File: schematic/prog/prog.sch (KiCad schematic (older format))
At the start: 24 parts

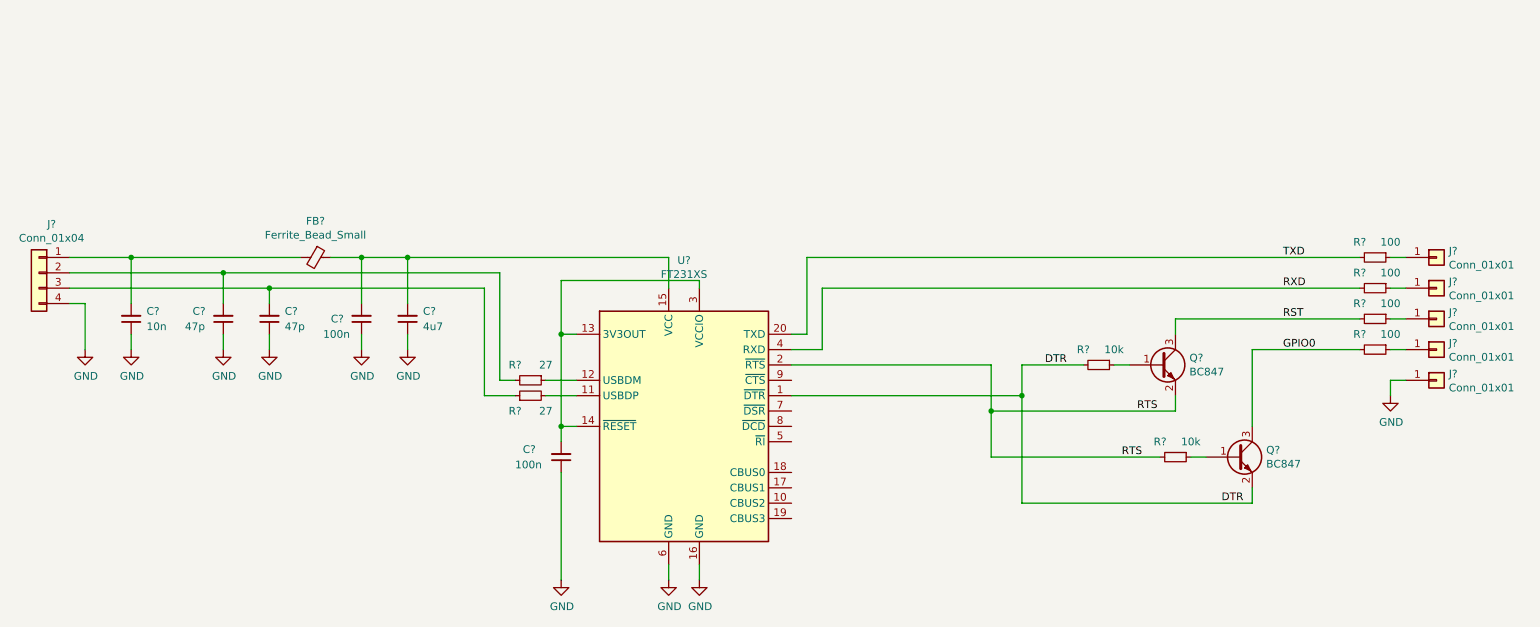
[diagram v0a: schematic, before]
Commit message: programing connector layout
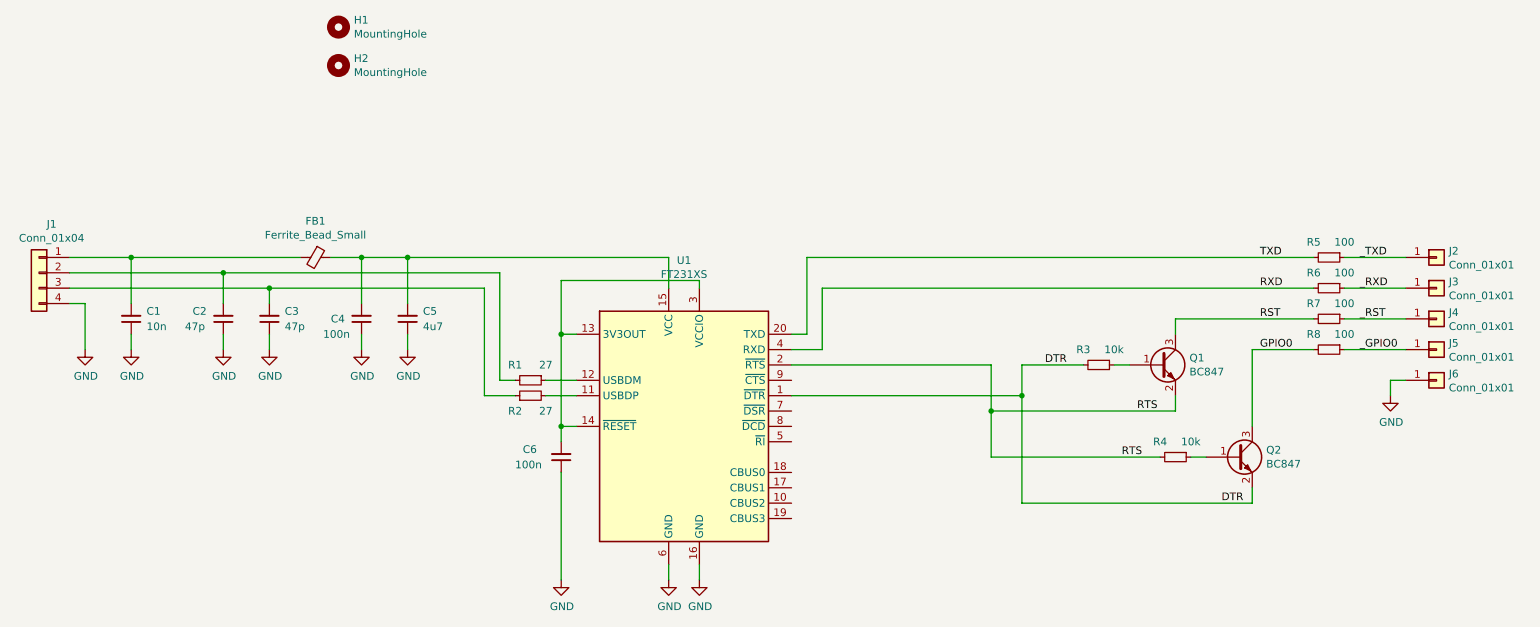
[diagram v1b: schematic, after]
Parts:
- added H1, H2: MountingHole, Mounting_Holes:MountingHole_2.2mm_M2, symbol Mechanical:MountingHole
- C1, C2, C3, C4, C6: renamed from C?; footprint (none) -> Capacitors_SMD:C_0603
- C5: renamed from C?; footprint (none) -> Capacitors_SMD:C_1206
- FB1: renamed from FB?; footprint (none) -> Resistors_SMD:R_0805
- J1: renamed from J?; footprint (none) -> keg01:SOLDER_CONN_4p
- J2, J3, J4, J5, J6: renamed from J?; footprint (none) -> keg01:POGO_FLAT
- Q1, Q2: renamed from Q?; footprint Package_TO_SOT_SMD:SOT-23 -> TO_SOT_Packages_SMD:SOT-23
- R1, R2, R3, R4, R5, R6, R7, R8: renamed from R?; footprint (none) -> Resistors_SMD:R_0603
- U1: renamed from U?; footprint Package_SO:SSOP-20_3.9x8.7mm_P0.635mm -> keg01:SSOP-20_3.9x8.7mm_P0.635mm
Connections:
- net _TXD: now reaches J2.1 (Pin_1), R5.1
- net _RXD: now reaches J3.1 (Pin_1), R6.1
- net _RST: now reaches J4.1 (Pin_1), R7.1
- net _GPIO0: now reaches J5.1 (Pin_1), R8.1
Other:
- moved on the sheet: R5, R6, R7, R8
